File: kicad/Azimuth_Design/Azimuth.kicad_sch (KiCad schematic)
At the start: 29 parts, among them IC1 BNO086, J1 TYPE-C 16PIN 2MD(073), U1 ESP32-C3-WROOM-02-N4(4MB)

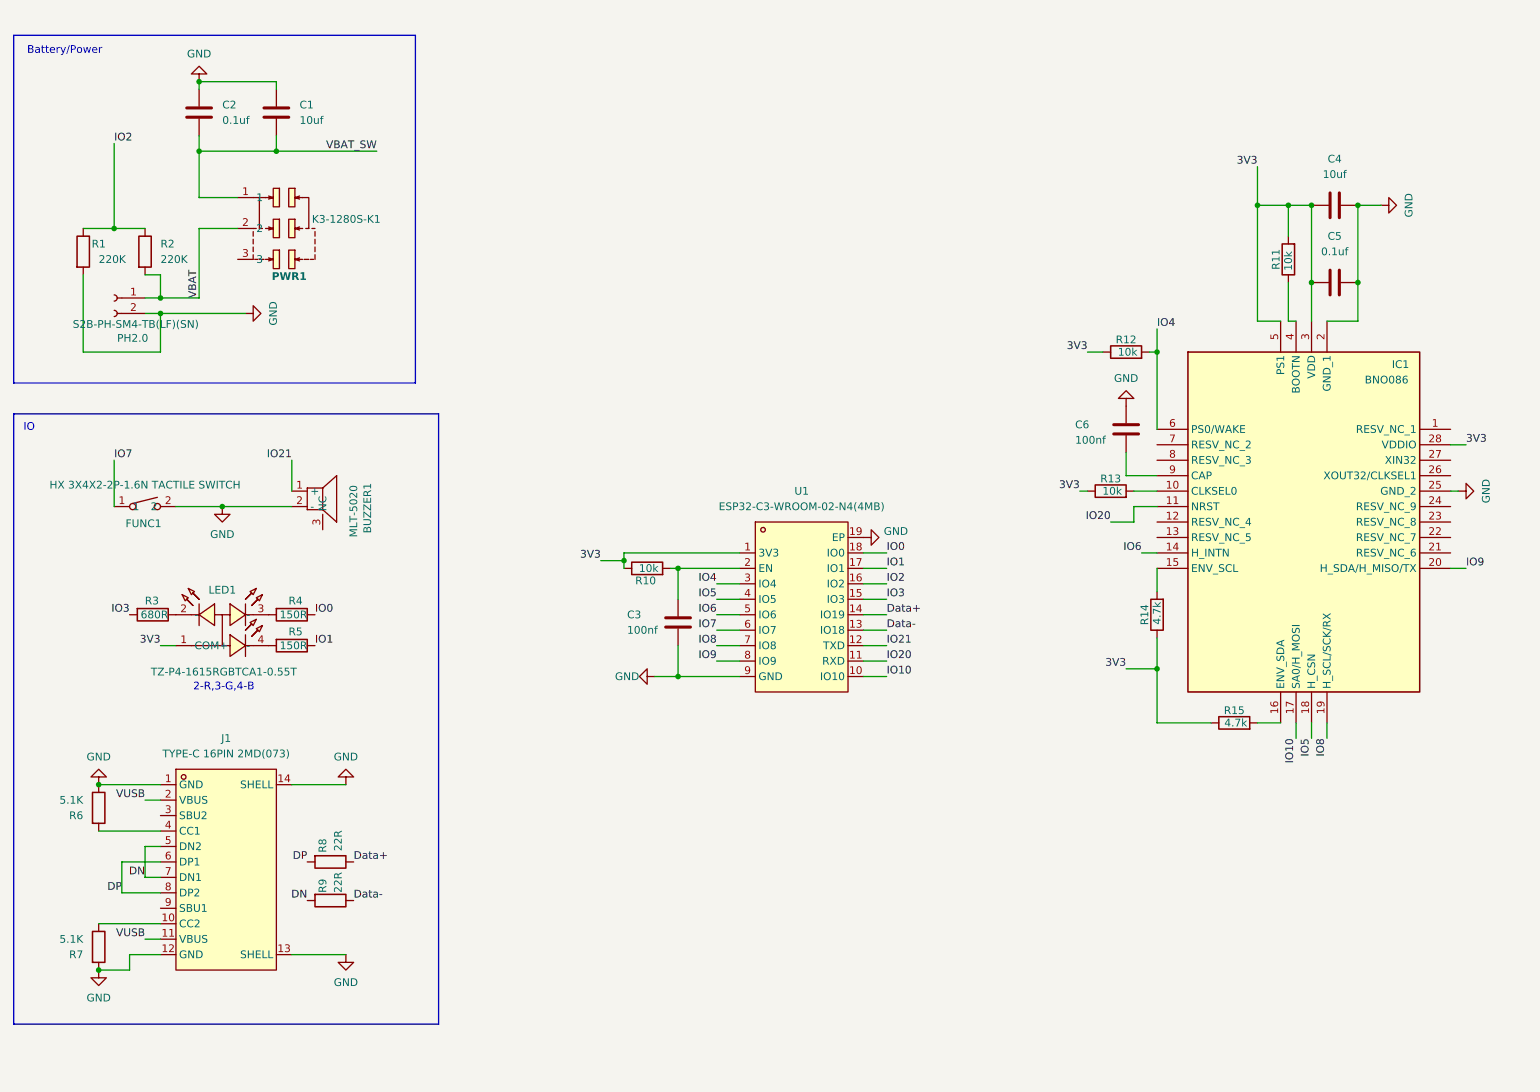
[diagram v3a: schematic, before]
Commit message: new PCB design almost done, big doc update
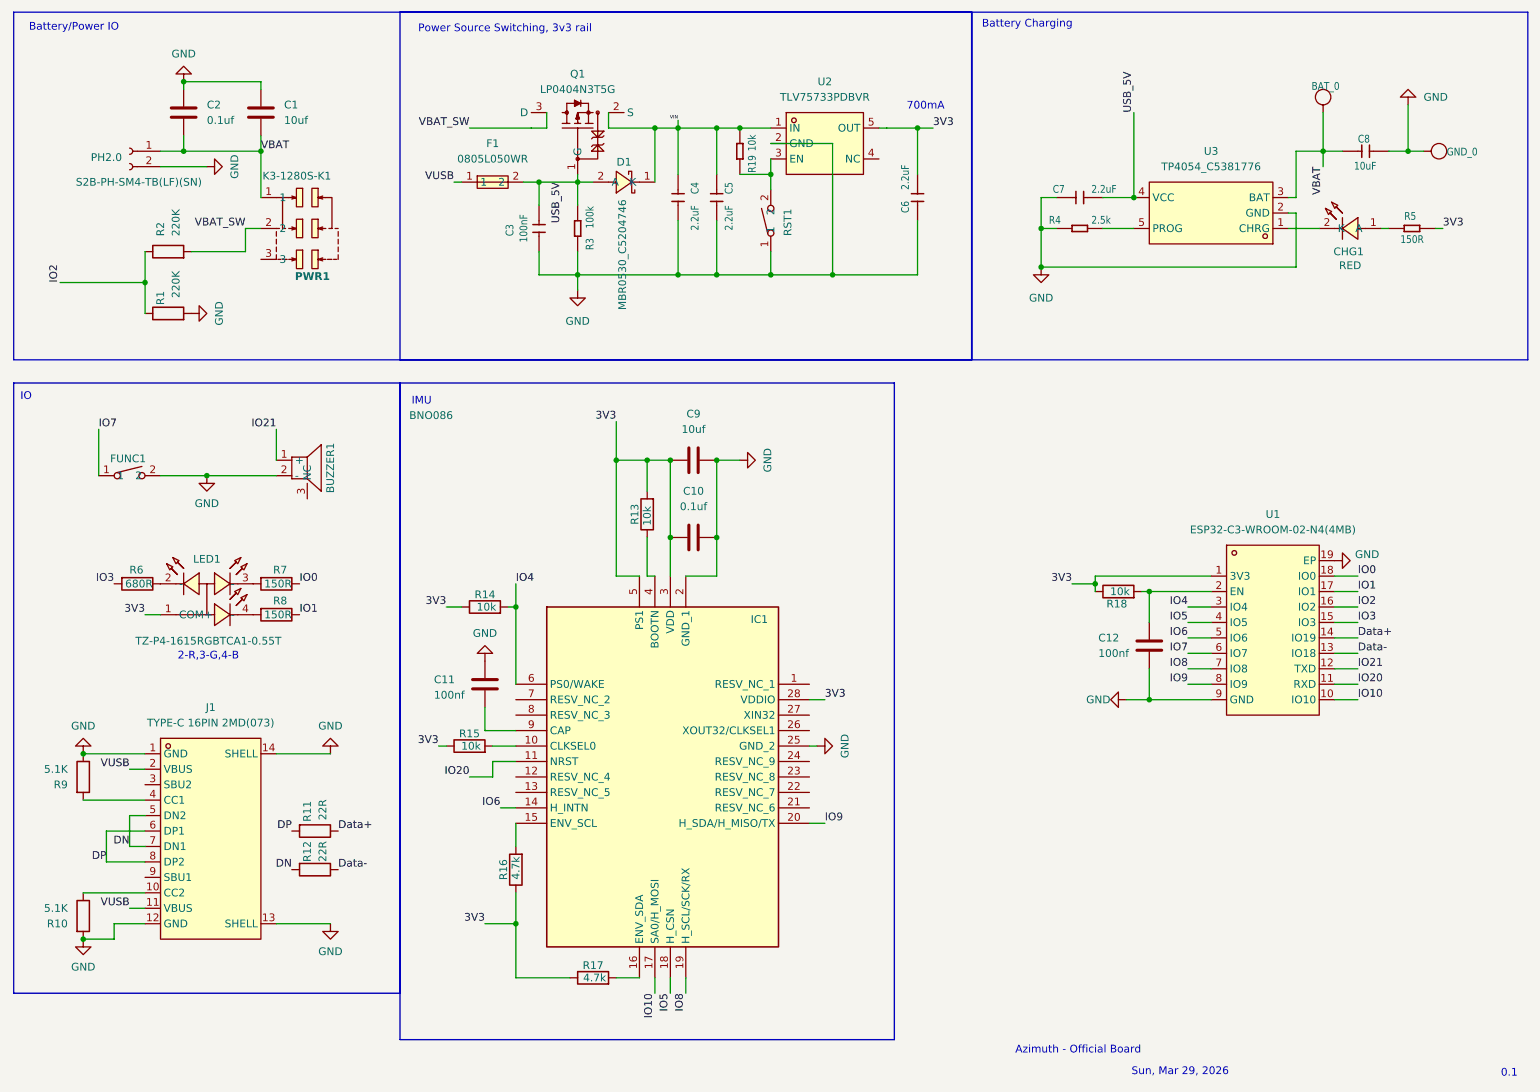
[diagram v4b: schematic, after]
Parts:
- added BAT_0, GND_0: DNP, TestPoint:TestPoint_Pad_D1.0mm, symbol XIAO ESP32C3_v1.3-eagle-import:TEST-POINT'4080'
- added C3: 100nF, Capacitor_SMD:C_0201_0603Metric, symbol XIAO ESP32C3_v1.3-eagle-import:CAP-0201
- added C4, C5, C6, C7: 2.2uF, Capacitor_SMD:C_0201_0603Metric, symbol XIAO ESP32C3_v1.3-eagle-import:CAP-0201
- added C8: 10uF, Capacitor_SMD:C_0201_0603Metric, symbol XIAO ESP32C3_v1.3-eagle-import:CAP-0201
- added CHG1: XL-0201SURC, 1_MyFootPrints:LED-SMD_L0.65-W0.35-P0.41_XL-0201SURC, symbol 1_MyLib:XL-0201SURC
- added D1: MBR0530_C5204746, 1_MyFootPrints:SOD-123_L2.7-W1.6-LS3.7-RD-1, symbol 1_MyLib:MBR0530_C5204746
- added F1: 0805L050WR, 1_MyFootPrints:R0805, symbol 1_MyLib:0805L050WR
- added FUNC1: HX 3X4X2-2P-1.6N TACTILE SWITCH, 1_MyFootPrints:KEY-SMD_L4.0-W3.0-LS4.9-1, symbol 1_MyLib:HX3X4X2-2P-1.6NTACTILESWITCH
- added Q1: LP0404N3T5G, 1_MyFootPrints:SOT-883-3_L1.0-W0.6-BR, symbol 1_MyLib:LP0404N3T5G
- added R19: 10k, Resistor_SMD:R_0201_0603Metric, symbol XIAO ESP32C3_v1.3-eagle-import:RES-0201
- added R3: 100k, Resistor_SMD:R_0201_0603Metric, symbol XIAO ESP32C3_v1.3-eagle-import:RES-0201
- added R4: 2.5k, Resistor_SMD:R_0201_0603Metric, symbol XIAO ESP32C3_v1.3-eagle-import:RES-0201
- added R5: 150R, Resistor_SMD:R_0201_0603Metric, symbol XIAO ESP32C3_v1.3-eagle-import:RES-0201
- added U2: TLV75733PDBVR, 1_MyFootPrints:SOT-23-5_L2.9-W1.6-P0.95-LS2.8-BL, symbol 1_MyLib:TLV75733PDBVR
- added U3: TP4054_C5381776, 1_MyFootPrints:SOT-23-5_L2.9-W1.6-P0.95-LS2.8-BR, symbol 1_MyLib:TP4054_C5381776
- C1: footprint Capacitor_SMD:C_0603_1608Metric -> Capacitor_SMD:C_0201_0603Metric; LCSC Part C19702 -> (none); Manufacturer_Part_Number CL10A106KP8NNNC -> (none)
- C10: renamed from C5; footprint Capacitor_SMD:C_0603_1608Metric -> Capacitor_SMD:C_0201_0603Metric; LCSC Part C14663 -> (none); Manufacturer_Part_Number CC0603KRX7R9BB104 -> (none)
- C11: renamed from C6; footprint Capacitor_SMD:C_0402_1005Metric -> Capacitor_SMD:C_0201_0603Metric; LCSC Part C77020 -> (none); Manufacturer_Part_Number GRM155R71H104KE14D -> (none)
- C12: renamed from C3; footprint Capacitor_SMD:C_0603_1608Metric -> Capacitor_SMD:C_0201_0603Metric
- C2: footprint Capacitor_SMD:C_0603_1608Metric -> Capacitor_SMD:C_0201_0603Metric; LCSC Part C14663 -> (none); Manufacturer_Part_Number CC0603KRX7R9BB104 -> (none)
- C9: renamed from C4; footprint Capacitor_SMD:C_0603_1608Metric -> Capacitor_SMD:C_0201_0603Metric; LCSC Part C19702 -> (none); Manufacturer_Part_Number CL10A106KP8NNNC -> (none)
- J1: footprint usb_type_c_C2765186:USB-C-SMD_TYPE-C-6PIN-2MD-073 -> 1_MyFootPrints:USB-C-SMD_TYPE-C-6PIN-2MD-073
- R1, R2: footprint Resistor_SMD:R_0603_1608Metric -> Resistor_SMD:R_0201_0603Metric; LCSC Part C2907013 -> (none); Manufacturer_Part_Number FRC0603F2203TS -> (none)
- R10: renamed from R7; footprint Resistor_SMD:R_0402_1005Metric -> Resistor_SMD:R_0201_0603Metric
- R11: renamed from R8; footprint Resistor_SMD:R_0402_1005Metric -> Resistor_SMD:R_0201_0603Metric
- R12: renamed from R9; footprint Resistor_SMD:R_0402_1005Metric -> Resistor_SMD:R_0201_0603Metric
- R13: renamed from R11; footprint Resistor_SMD:R_0402_1005Metric -> Resistor_SMD:R_0201_0603Metric; LCSC Part C60490 -> (none); Manufacturer_Part_Number RC0402FR-0710KL -> (none)
- R14: renamed from R12; footprint Resistor_SMD:R_0402_1005Metric -> Resistor_SMD:R_0201_0603Metric; LCSC Part C60490 -> (none); Manufacturer_Part_Number RC0402FR-0710KL -> (none)
- R15: renamed from R13; footprint Resistor_SMD:R_0402_1005Metric -> Resistor_SMD:R_0201_0603Metric; LCSC Part C60490 -> (none); Manufacturer_Part_Number RC0402FR-0710KL -> (none)
- R16: renamed from R14; footprint Resistor_SMD:R_0402_1005Metric -> Resistor_SMD:R_0201_0603Metric; LCSC Part C105871 -> (none); Manufacturer_Part_Number RC0402FR-074K7L -> (none)
- R17: renamed from R15; footprint Resistor_SMD:R_0402_1005Metric -> Resistor_SMD:R_0201_0603Metric; LCSC Part C105871 -> (none); Manufacturer_Part_Number RC0402FR-074K7L -> (none)
- R18: renamed from R10; footprint Resistor_SMD:R_0402_1005Metric -> Resistor_SMD:R_0201_0603Metric; LCSC Part C60490 -> (none); Manufacturer_Part_Number RC0402FR-0710KL -> (none)
- R6: renamed from R3; footprint Resistor_SMD:R_0402_1005Metric -> Resistor_SMD:R_0201_0603Metric
- R7: renamed from R4; footprint Resistor_SMD:R_0402_1005Metric -> Resistor_SMD:R_0201_0603Metric
- R8: renamed from R5; footprint Resistor_SMD:R_0402_1005Metric -> Resistor_SMD:R_0201_0603Metric
- R9: renamed from R6; footprint Resistor_SMD:R_0402_1005Metric -> Resistor_SMD:R_0201_0603Metric
- U1: footprint easyeda2kicad:BULETM-SMD_ESPRESSIF_ESP32-C3-WROOM-02-N4-4MB -> 1_MyFootPrints:BULETM-SMD_ESPRESSIF_ESP32-C3-WROOM-02-N4-4MB
- renumbered FUNC1 to RST1
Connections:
- net 3V3: now also C6.2, R5.1, U2.5 (OUT)
- net GND: now also RST1.1, C3.1, C4.2, C5.2, C6.1, C7.1, C8.2, FUNC1.2, GND_0.1 (T), R3.1, R4.2, U2.2 (GND), U3.2 (GND); no longer RST1.2
- net IO7: now also FUNC1.1; no longer RST1.1
- net VBAT: now also C1.2, C2.1, PWR1.1, BAT_0.1 (T), C8.1, U3.3 (BAT); no longer PWR1.2, R2.2
- net VBAT_SW: now also PWR1.2, R2.2, Q1.3 (D); no longer C1.2, C2.1, PWR1.1
- net VUSB: now also F1.1
- new net: R4.1, U3.5 (PROG)
- new net: CHG1.1 (A), R5.2
- new net: CHG1.2 (K), U3.1 (CHRG)
- new net: R19.1, RST1.2, U2.3 (EN)
- new net USB_5V: C3.2, C7.2, D1.2 (A), F1.2, Q1.1 (G), R3.2, U3.4 (VCC)
- new net VIN: C4.1, C5.1, D1.1 (K), Q1.2 (S), R19.2, U2.1 (IN)
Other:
- note added: "0.1"
- note added: "700mA"
- note added: "Azimuth - Official Board"
- note added: "Battery Charging"
- note added: "Battery/Power IO"
- note added: "IMU"
- note added: "Power Source Switching, 3v3 rail"
- note added: "Sun, Mar 29, 2026"
- note removed: "Battery/Power"
- moved on the sheet: BUZZER1, C1, C10, C11, C12, C2, C9, IC1, J1, LED1, PH2.0, PWR1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

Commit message: PCB locked in for now, docs updated
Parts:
- added D2: B5819WS, 1_MyFootPrints:SOD-323_L1.8-W1.3-LS2.5-RD, symbol 1_MyLib:B5819WS
- added Q2: AO3400A, 1_MyFootPrints:SOT-23-3_L2.9-W1.3-P1.90-LS2.4-BR, symbol 1_MyLib:AO3400A
- added R20: 330R, Resistor_SMD:R_0201_0603Metric, symbol XIAO ESP32C3_v1.3-eagle-import:RES-0201
- added R21: 100K, Resistor_SMD:R_0201_0603Metric, symbol XIAO ESP32C3_v1.3-eagle-import:RES-0201
- C1, C8, C9: footprint Capacitor_SMD:C_0201_0603Metric -> Capacitor_SMD:C_0402_1005Metric; LCSC Part (none) -> C315248; Manufacturer_Part_Number (none) -> CL05A106MP5NUNC
- C10, C2: footprint Capacitor_SMD:C_0201_0603Metric -> Capacitor_SMD:C_0402_1005Metric; LCSC Part (none) -> C60474; Manufacturer_Part_Number (none) -> CC0402KRX7R7BB104
- C11, C12, C3: LCSC Part (none) -> C76934; Manufacturer_Part_Number (none) -> GRM033R61A104KE15D
- C4, C5, C6, C7: LCSC Part (none) -> C335106; Manufacturer_Part_Number (none) -> GRM033R61A225KE47D
- CHG1: Manufacturer_Part_Number (none) -> XL-0201SURC
- D1: Manufacturer_Part_Number (none) -> MBR0530
- F1: Manufacturer_Part_Number (none) -> 0805L050WR
- Q1: Manufacturer_Part_Number (none) -> LP0404N3T5G
- R1, R2: footprint Resistor_SMD:R_0201_0603Metric -> Resistor_SMD:R_0402_1005Metric; LCSC Part (none) -> C25767; Manufacturer_Part_Number (none) -> 0402WGF2203TCE
- R10, R9: LCSC Part (none) -> C274341; Manufacturer_Part_Number (none) -> RC0201FR-075K1L
- R11, R12: LCSC Part (none) -> C155743; Manufacturer_Part_Number (none) -> RC0201FR-0722RL
- R13, R14, R15, R18, R19: LCSC Part (none) -> C106225; Manufacturer_Part_Number (none) -> RC0201FR-0710KL
- R16, R17: LCSC Part (none) -> C138135; Manufacturer_Part_Number (none) -> RC0201FR-074K7L
- R3: LCSC Part (none) -> C106224; Manufacturer_Part_Number (none) -> RC0201FR-07100KL
- R4: value 2.5k -> 2K; LCSC Part (none) -> C327392; Manufacturer_Part_Number (none) -> RC0201FR-072KL
- R5, R7, R8: LCSC Part (none) -> C295773; Manufacturer_Part_Number (none) -> RC0201FR-07150RL
- R6: LCSC Part (none) -> C274876; Manufacturer_Part_Number (none) -> RC0201FR-07680RL
- U2: Manufacturer_Part_Number (none) -> TLV75733PDBVR
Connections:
- net 3V3: now also BUZZER1.1 (+), D2.1 (K)
- net GND: now also Q2.2 (S), R21.2; no longer BUZZER1.2 (-)
- net IO21: now also R20.2; no longer BUZZER1.1 (+)
- new net: BUZZER1.2 (-), D2.2 (A), Q2.3 (D)
- new net: Q2.1 (G), R20.1, R21.1
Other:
- moved on the sheet: BUZZER1, FUNC1, LED1, R6, R7, R8

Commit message: PCB finalized? :O
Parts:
- removed BAT_0, GND_0: DNP, TestPoint:TestPoint_Pad_D1.0mm, symbol XIAO ESP32C3_v1.3-eagle-import:TEST-POINT'4080'
- added Q3: AO3401A, 1_MyFootPrints:SOT-23-3_L2.9-W1.3-P1.90-LS2.4-BR, symbol 1_MyLib:AO3401A
- added R22: 100k, Resistor_SMD:R_0201_0603Metric, symbol XIAO ESP32C3_v1.3-eagle-import:RES-0201
- BUZZER1: Unit Price (USD) (none) -> 0.4246
- C1, C9: Unit Price (USD) (none) -> 0.0087
- C10, C2, R16, R17, R3: Unit Price (USD) (none) -> 0.001
- C11, C12: Unit Price (USD) (none) -> 0.002
- C3: value 100nF -> 100nf; Unit Price (USD) (none) -> 0.002
- C4, C5, C6, C7: value 2.2uF -> 2.2uf; Unit Price (USD) (none) -> 0.0212
- C8: value 10uF -> 10uf; Unit Price (USD) (none) -> 0.0087
- CHG1: Unit Price (USD) (none) -> 0.069
- D1: Unit Price (USD) (none) -> 0.0193
- D2: Unit Price (USD) (none) -> 0.0217
- F1: Unit Price (USD) (none) -> 0.1119
- FUNC1, RST1: Unit Price (USD) (none) -> 0.0186
- IC1: DigiKey Link (none) -> https://www.digikey.com/en/products/detail/ceva-technologie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; DigiKey Part Number (none) -> 1888-BNO086TR-ND; Unit Price (USD) (none) -> 11.50
- J1: Manufacturer (none) -> SHOU HAN; Unit Price (USD) (none) -> 0.0649
- LED1: Unit Price (USD) (none) -> 0.0244
- PH2.0: Unit Price (USD) (none) -> 0.1947
- PWR1: Unit Price (USD) (none) -> 0.1791
- Q1: Unit Price (USD) (none) -> 0.0267
- Q2: Unit Price (USD) (none) -> 0.0798
- R1, R2: value 220K -> 220k; Unit Price (USD) (none) -> 0.0007
- R10, R9: value 5.1K -> 5.1k; Unit Price (USD) (none) -> 0.0011
- R11, R12, R13, R14, R15, R18, R19, R20, R4, R5, R6, R7, R8: Unit Price (USD) (none) -> 0.0011
- R21: value 100K -> 100k; Unit Price (USD) (none) -> 0.001
- U1: Unit Price (USD) (none) -> 3.0674
- U2: Unit Price (USD) (none) -> 0.1959
- U3: Unit Price (USD) (none) -> 0.0145
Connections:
- net GND: now also PH2.0.1 (Pin_1), R22.1; no longer J1.13 (SHELL), J1.14 (SHELL), PH2.0.2 (Pin_2)
- net IO2: now also IC1.6 (PS0/WAKE), R14.2; no longer R1.1, R2.1
- net IO4: now also R1.1, R2.1; no longer IC1.6 (PS0/WAKE), R14.2
- net VBAT: now also Q3.3 (D); no longer PH2.0.1 (Pin_1)
- new net: Q3.1 (G), R22.2
- new net: PH2.0.2 (Pin_2), Q3.2 (S)
- no-connect marks 0 -> 16
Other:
- moved on the sheet: C1, C2, PH2.0, PWR1, R1, R2

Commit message: Manufacturing optimizations
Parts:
- R6: value 680R -> 220R; LCSC Part C274876 -> C49654383; Manufacturer_Part_Number RC0201FR-07680RL -> GR0201F220RTAG00; Unit Price (USD) 0.0011 -> 0.0006
- R7: value 150R -> 100R; LCSC Part C295773 -> C77623; Manufacturer_Part_Number RC0201FR-07150RL -> RC0201FR-07100RL
- R8: value 150R -> 68R; LCSC Part C295773 -> C49655823; Manufacturer_Part_Number RC0201FR-07150RL -> GR0201J68RTAG00; Unit Price (USD) 0.0011 -> 0.001
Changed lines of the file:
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@@
 			)
 		)
-		(property "Description" "Battery divider low side: VBAT/2 tap to IO4 for ADC (with R1)"
+		(property "Description" "Battery divider low side: VBAT_SW tap to IO4 for ADC (with R1)"
 			(at 43.18 55.88 0)
 			(effects
@@
 			)
 		)
-		(property "Description" "PS0/WAKE pull-up to 3V3 on IO2 (BNO086 SPI strap + ESP32 strap GPIO2 high)"
+		(property "Description" "PS0/WAKE pull-up to 3V3 on IO2 (BNO086 SPI strap + ESP32 GPIO2)"
 			(at 101.6 116.84 0)
 			(effects
@@
 			)
 		)
-		(property "Value" "680R"
+		(property "Value" "220R"
 			(at 46.99 116.84 90)
 			(effects
@@
 			)
 		)
-		(property "Description" "RGB LED blue cathode resistor (IO3): lower current for brightness balance"
+		(property "Description" "RGB LED blue cathode resistor (IO3); tuned with R7/R8 for TZ-P4-1615RGBTCA1 balance on 3V3"
 			(at 44.45 116.84 0)
 			(effects
@@
 			)
 		)
-		(property "Manufacturer_Part_Number" "RC0201FR-07680RL"
+		(property "Manufacturer_Part_Number" "GR0201F220RTAG00"
 			(at 44.45 116.84 0)
 			(effects
@@
 			)
 		)
-		(property "LCSC Part" "C274876"
+		(property "LCSC Part" "C49654383"
 			(at 44.45 116.84 0)
 			(effects
@@
 			)
 		)
-		(property "Unit Price (USD)" "0.0011"
+		(property "Unit Price (USD)" "0.0006"
 			(at 0 0 0)
 			(effects
@@
 			)
 		)
-		(property "Value" "150R"
+		(property "Value" "68R"
 			(at 69.85 121.92 90)
 			(effects
@@
 			)
 		)
-		(property "Manufacturer_Part_Number" "RC0201FR-07150RL"
+		(property "Manufacturer_Part_Number" "GR0201J68RTAG00"
 			(at 67.31 121.92 0)
 			(effects
@@
 			)
 		)
-		(property "LCSC Part" "C295773"
+		(property "LCSC Part" "C49655823"
 			(at 67.31 121.92 0)
 			(effects
@@
 			)
 		)
-		(property "Unit Price (USD)" "0.0011"
+		(property "Unit Price (USD)" "0.001"
 			(at 0 0 0)
 			(effects
@@
 			)
 		)
-		(property "Description" "USB_5V (post-fuse VBUS) HF bypass to GND — not IMU rail"
+		(property "Description" "USB_5V (post-fuse VBUS) HF bypass to GND"
 			(at 110.49 54.61 0)
 			(effects
@@
 			)
 		)
-		(property "Value" "150R"
+		(property "Value" "100R"
 			(at 69.85 116.84 90)
 			(effects
@@
 			)
 		)
-		(property "Manufacturer_Part_Number" "RC0201FR-07150RL"
+		(property "Manufacturer_Part_Number" "RC0201FR-07100RL"
 			(at 67.31 116.84 0)
 			(effects
@@
 			)
 		)
-		(property "LCSC Part" "C295773"
+		(property "LCSC Part" "C77623"
 			(at 67.31 116.84 0)
 			(effects
